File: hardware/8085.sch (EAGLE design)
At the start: 52 parts, among them IC10 74HCT00N, IC11 74HCT245DW, IC2 74AC573N, IC3 ATF16V8BP3, IC4 74AC00D, IC5 74HCT245DW, IC6 74AC273N, IC7 74HCT139N, IC8 7404N, IC9 74HCT138N

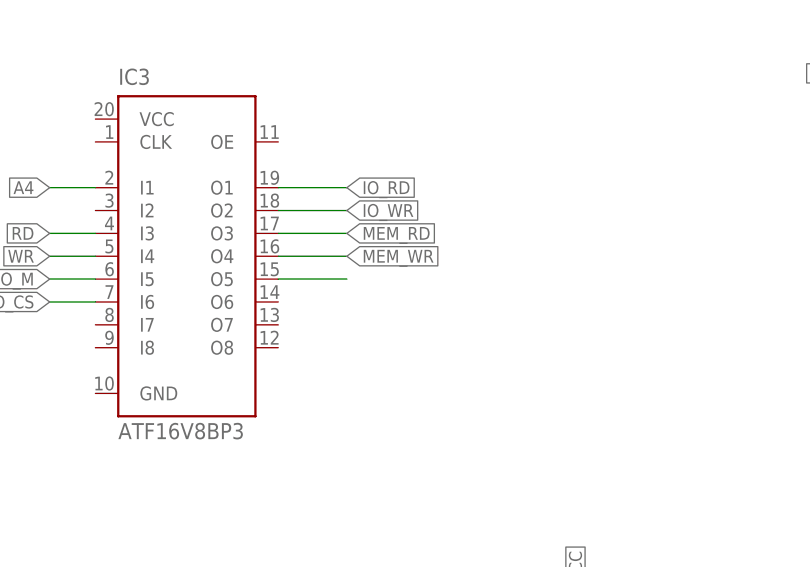
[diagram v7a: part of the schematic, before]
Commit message: HW bug fixed, GAL added
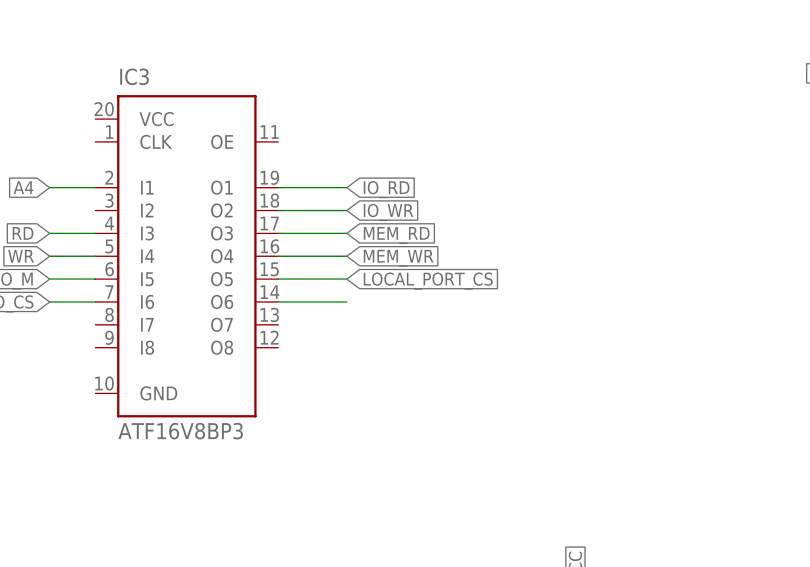
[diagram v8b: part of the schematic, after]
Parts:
- R11, R7: device rcl:R-EU_0204/7 -> rcl:R-EU_0207/10
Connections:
- net CF_CS0: now also IC3.O6
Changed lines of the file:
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@@
 <part name="GND19" library="supply1" deviceset="GND" device=""/>
 <part name="GND20" library="supply1" deviceset="GND" device=""/>
-<part name="R7" library="rcl" deviceset="R-EU_" device="0204/7"/>
+<part name="R7" library="rcl" deviceset="R-EU_" device="0207/10"/>
 <part name="R8" library="rcl" deviceset="R-EU_" device="0207/10"/>
 <part name="R10" library="rcl" deviceset="R-EU_" device="0207/10"/>
-<part name="R11" library="rcl" deviceset="R-EU_" device="0204/7"/>
+<part name="R11" library="rcl" deviceset="R-EU_" device="0207/10"/>
 <part name="RN1" library="resistor-sil" deviceset="G04R" device=""/>
 <part name="R1" library="rcl" deviceset="R-EU_" device="0204/5"/>
@@
 <pinref part="IC3" gate="G$1" pin="O5"/>
 <wire x1="68.58" y1="-93.98" x2="76.2" y2="-93.98" width="0.1524" layer="91"/>
+<label x="76.2" y="-93.98" size="1.4224" layer="95" xref="yes"/>
 </segment>
 </net>
@@
 <label x="200.66" y="-259.08" size="1.4224" layer="95" rot="R180" xref="yes"/>
 </segment>
-</net>
+<segment>
+<pinref part="IC3" gate="G$1" pin="O6"/>
+<wire x1="68.58" y1="-96.52" x2="76.2" y2="-96.52" width="0.1524" layer="91"/>
+</segment>
+</net>
